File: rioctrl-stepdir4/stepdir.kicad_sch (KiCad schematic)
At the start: 19 parts, among them J3 RJ45_LED_Shielded, Q5 BSS138W, Q6 AO3401A, U1 CS48505S, U2 CS48505S, U6 USBLC6-4SC6

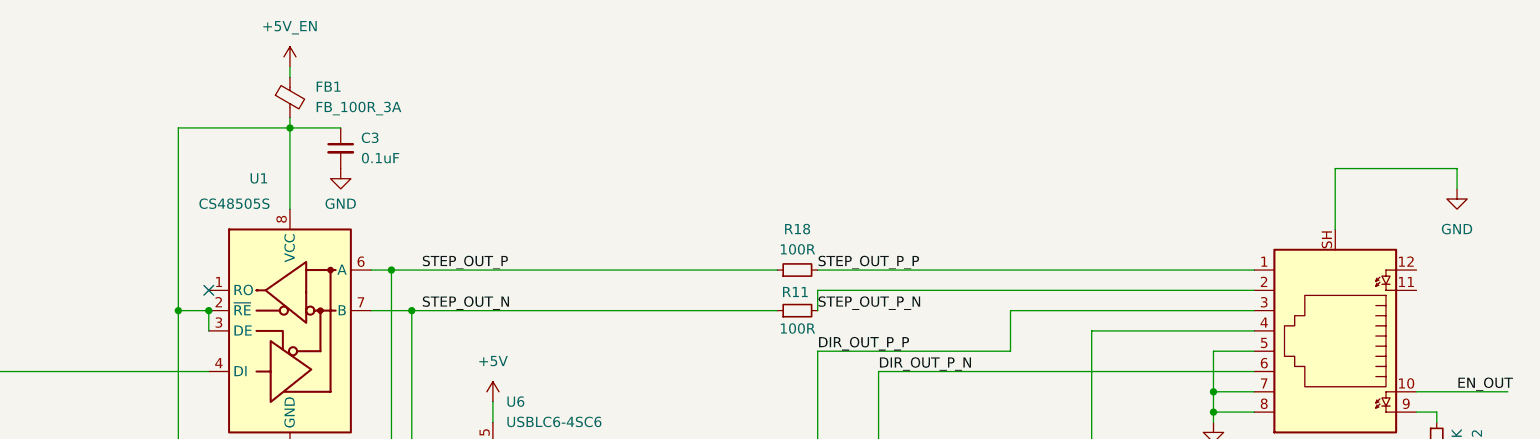
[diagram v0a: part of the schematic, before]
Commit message: rioctrl-stepdir4: pass ERC and DRC
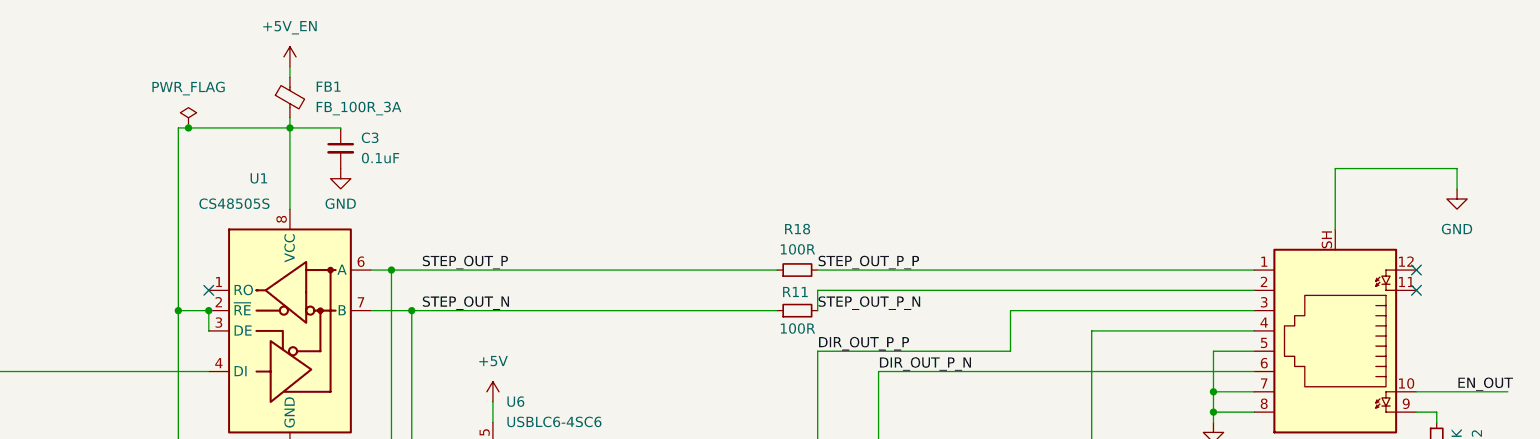
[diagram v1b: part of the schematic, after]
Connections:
- no-connect marks 2 -> 4
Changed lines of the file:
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@@
 	)
 	(junction
+		(at 86.36 26.67)
+		(diameter 0)
+		(color 0 0 0 0)
+	)
+	(junction
 		(at 114.3 49.53)
 		(diameter 0)
@@
 		(at 88.9 46.99)
 	)
+	(no_connect
+		(at 240.03 46.99)
+	)
+	(no_connect
+		(at 240.03 44.45)
+	)
 	(wire
 		(pts
@@
 	(wire
 		(pts
-			(xy 85.09 26.67) (xy 99.06 26.67)
+			(xy 85.09 26.67) (xy 86.36 26.67)
 		)
 		(stroke
@@
 	(wire
 		(pts
+			(xy 86.36 26.67) (xy 99.06 26.67)
+		)
+		(stroke
+			(width 0)
+			(type default)
+		)
+	)
+	(wire
+		(pts
 			(xy 240.03 59.69) (xy 251.46 59.69)
 		)
@@
 			)
 		)
-		(property "Description" ""
+		(property "Description" "Power symbol creates a global label with name \"GND\" , ground"
 			(at 99.06 124.46 0)
 			(effects
@@
 	)
 	(symbol
+		(lib_id "power:PWR_FLAG")
+		(at 86.36 26.67 0)
+		(unit 1)
+		(exclude_from_sim no)
+		(in_bom yes)
+		(on_board yes)
+		(dnp no)
+		(fields_autoplaced yes)
+		(property "Reference" "#FLG07"
+			(at 86.36 24.765 0)
+			(effects
+				(font
+					(size 1.27 1.27)
+				)
+				(hide yes)
+			)
+		)
+		(property "Value" "PWR_FLAG"
+			(at 86.36 21.59 0)
+			(effects
+				(font
+					(size 1.27 1.27)
+				)
+			)
+		)
+		(property "Footprint" ""
+			(at 86.36 26.67 0)
+			(effects
+				(font
+					(size 1.27 1.27)
+				)
+				(hide yes)
+			)
+		)
+		(property "Datasheet" "~"
+			(at 86.36 26.67 0)
+			(effects
+				(font
+					(size 1.27 1.27)
+				)
+				(hide yes)
+			)
+		)
+		(property "Description" "Special symbol for telling ERC where power comes from"
+			(at 86.36 26.67 0)
+			(effects
+				(font
+					(size 1.27 1.27)
+				)
+				(hide yes)
+			)
+		)
+		(pin "1"
+		)
+		(instances
+			(project "rioctrl-stepdir4"
+				(path "/09587842-9628-4761-8ca3-5c7cdb77bd67/05836d8b-9c0a-4ec5-b5c3-59f72c542683"
+					(reference "#FLG09")
+					(unit 1)
+				)
+				(path "/09587842-9628-4761-8ca3-5c7cdb77bd67/37660470-539d-4ef0-8319-4a3363bab027"
+					(reference "#FLG010")
+					(unit 1)
+				)
+				(path "/09587842-9628-4761-8ca3-5c7cdb77bd67/6edbf5bb-a097-4513-bbfc-fc51b4716a77"
+					(reference "#FLG08")
+					(unit 1)
+				)
+				(path "/09587842-9628-4761-8ca3-5c7cdb77bd67/eebf3392-0a38-4e82-919d-cd3d193b6f43"
+					(reference "#FLG07")
+					(unit 1)
+				)
+			)
+		)
+	)
+	(symbol
 		(lib_id "power:GND")
 		(at 105.41 88.9 0)
@@
 			)
 		)
-		(property "Description" ""
+		(property "Description" "Power symbol creates a global label with name \"GND\" , ground"
 			(at 105.41 88.9 0)
 			(effects
@@
 			)
 		)
-		(property "Description" ""
+		(property "Description" "Power symbol creates a global label with name \"GND\" , ground"
 			(at 99.06 67.31 0)
 			(effects
@@
 	)
 	(symbol
-		(lib_name "GND_1")
 		(lib_id "power:GND")
 		(at 242.57 68.58 0)
@@
 			)
 		)
-		(property "Description" ""
+		(property "Description" "Power symbol creates a global label with name \"GND\" , ground"
 			(at 105.41 31.75 0)
 			(effects
@@
 			)
 		)
-		(property "Description" ""
+		(property "Description" "Power symbol creates a global label with name \"GND\" , ground"
 			(at 100.33 180.34 0)
 			(effects
@@
 			)
 		)
-		(property "Description" ""
+		(property "Description" "Power symbol creates a global label with name \"GND\" , ground"
 			(at 80.01 172.72 0)
 			(effects
@@
 	)
 	(symbol
-		(lib_name "GND_2")
 		(lib_id "power:GND")
 		(at 214.63 63.5 0)
@@
 	)
 	(symbol
-		(lib_name "GND_1")
 		(lib_id "power:GND")
 		(at 245.11 34.29 0)
@@
 	)
 	(symbol
-		(lib_name "GND_2")
 		(lib_id "power:GND")
 		(at 124.46 83.82 0)
